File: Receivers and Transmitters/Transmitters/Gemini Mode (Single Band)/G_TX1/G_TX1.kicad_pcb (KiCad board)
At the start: 4 copper layers, 39.8 x 55.8 mm, 37 parts, among them J1 Conn_01x05_Socket, J2 Conn_01x03_Socket, J3 Conn_01x04_Socket, J4 Conn_02x06_Odd_Even, U1 TPS7A4701xRGW, U2 ESP32-WROOM-32, U3 E28-2G4M27S, U4 ESP8285H16, U5 E28-2G4M27S, Y2 26MHz

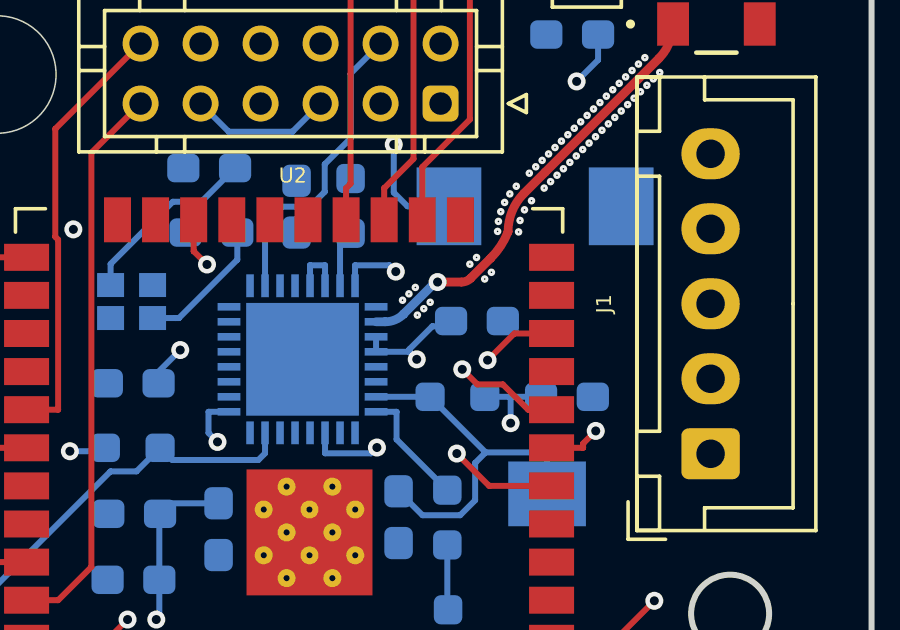
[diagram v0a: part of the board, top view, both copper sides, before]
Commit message: Add Gemini Mode (Single Band) TX board image and documentation updates - Updated hardware setup to include Gemini TX - Added G_TX1_2.4G preview image - Updated KiCad schematic with LNA section and 5.6pF matching capacitor for 50Ω impedance - Modified PCB layout accordingly - Updated README and index.html with Gemini TX board references
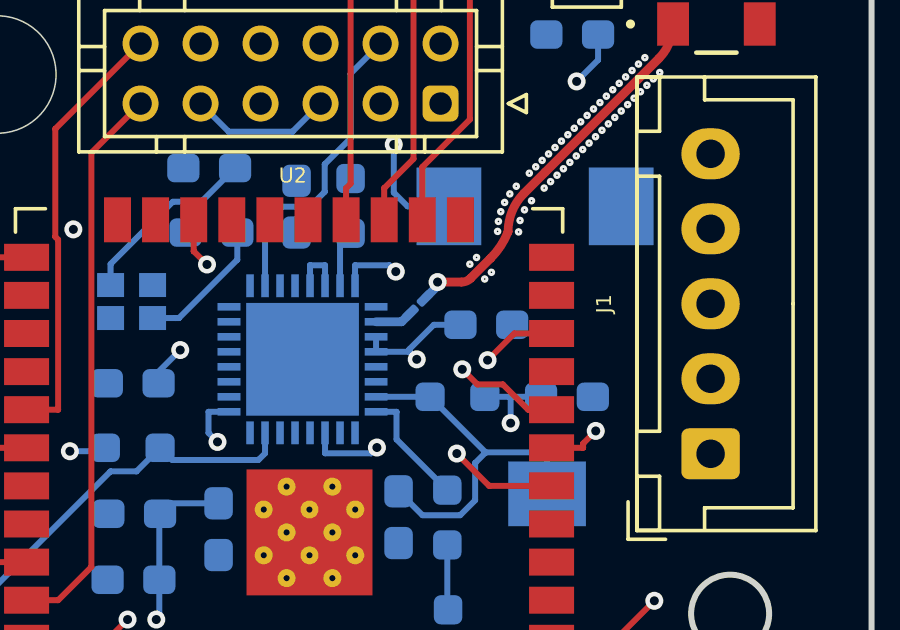
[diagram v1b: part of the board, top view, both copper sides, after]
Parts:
- added C33: 5.6pF, Capacitor_SMD:C_01005_0402Metric_Pad0.57x0.30mm_HandSolder, B.Cu at (153.8, 89.0)
- moved C28 0.34 mm to (156.1, 89.7)
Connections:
- AE1 pad 1: Net-(U4-LNA) -> Net-(AE1-Pad1)
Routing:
- net Net-(U4-LNA): track 14.7 -> 1.27 mm, vias 1 -> 0
- net Net-(AE1-Pad1): track 0.00 -> 13.0 mm, vias 0 -> 1
- net GND: vias 58 -> 52

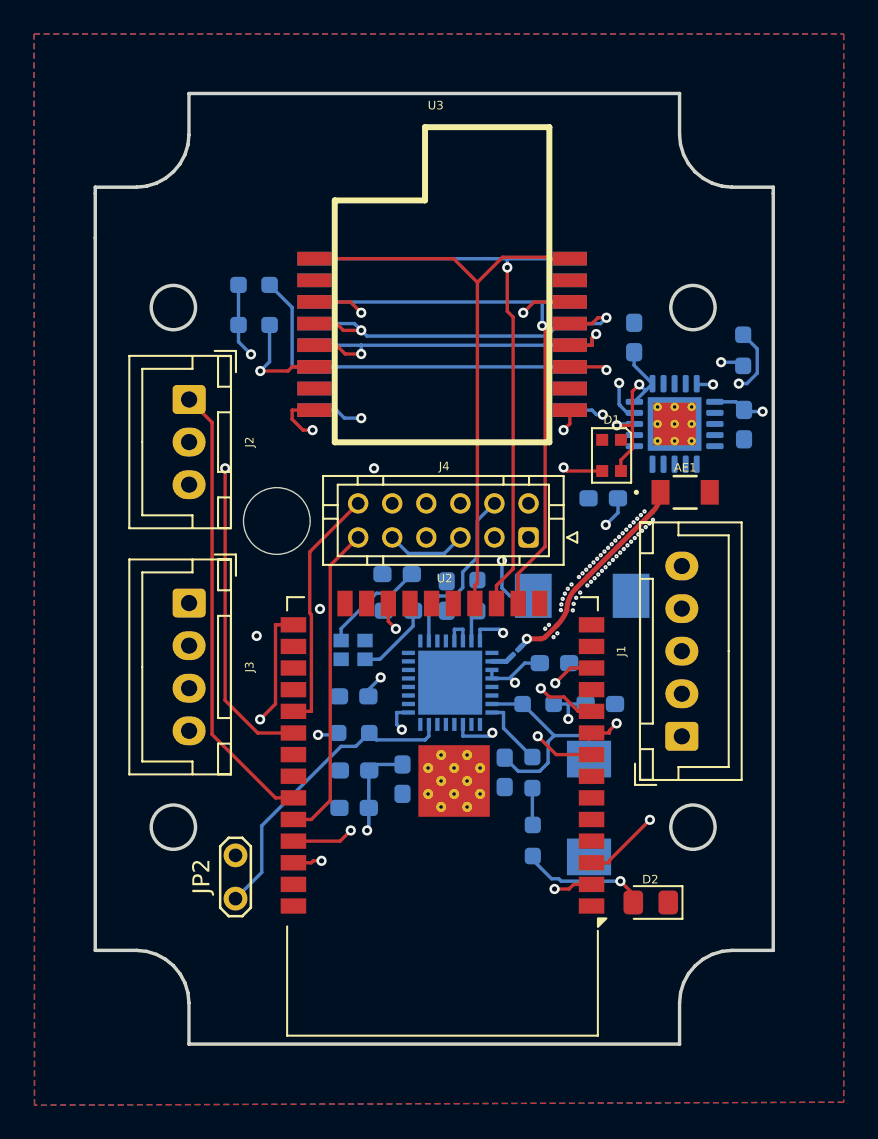
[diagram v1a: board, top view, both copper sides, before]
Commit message: Update Antenna Diversity (AD1_2.4G), True Antenna Diversity (TD1_2.4G), and Gemini Mode transmitter (G_TX1): Modify KiCad files, add BOMs and production files; update images, docs, videos, and README; remove outdated Mechanical CAD file
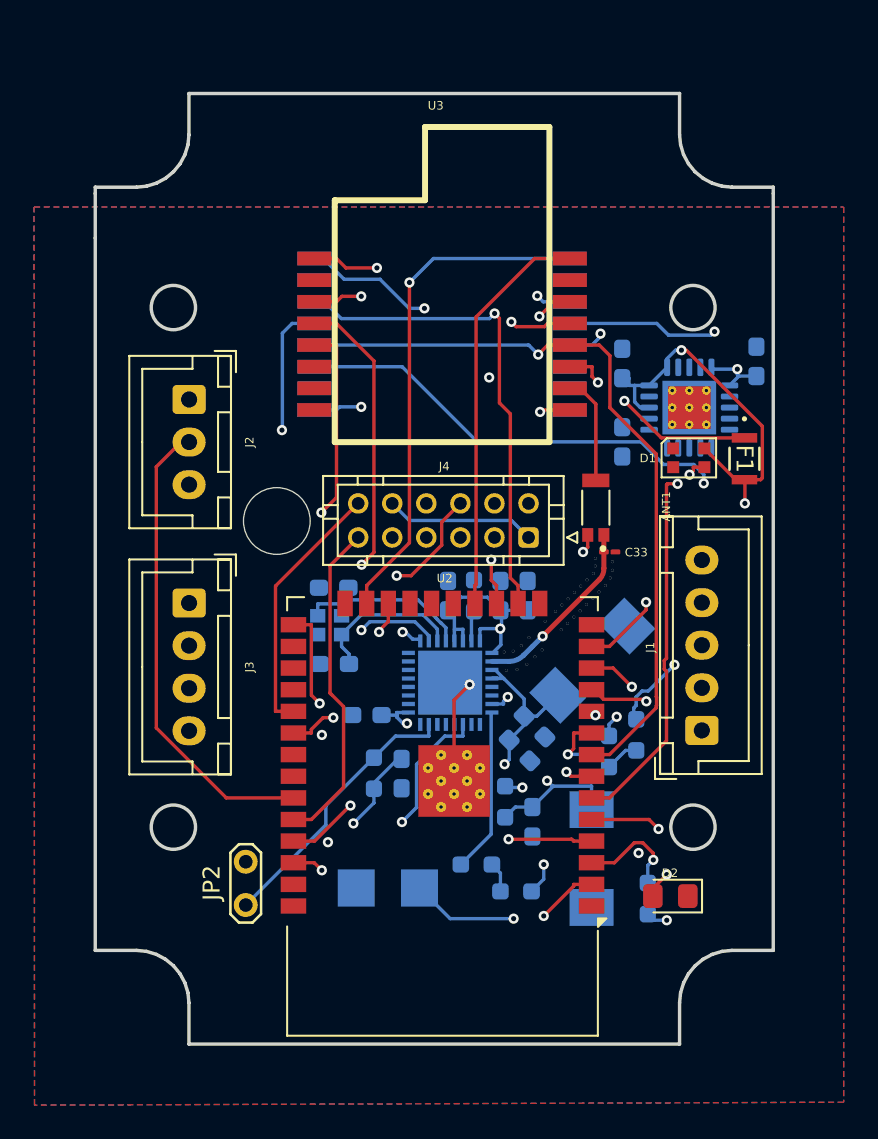
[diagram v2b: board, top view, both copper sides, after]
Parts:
- removed AE1: W3008, W3008:ANT_W3008_PUL
- added ANT1: W3008, W3008:ANTENNA_W3008, F.Cu at (158.5, 80.5)
- added CR1: SMBJ60A, ul_SMBJ60A:SMBJSeries_LTF, B.Cu at (146.3, 102.8)
- added F1: MF-PSMF020X-2, ul_MF-PSMF020X-2:FUSE_F020X_BRN, F.Cu at (167.2, 77.7)
- added QR*****: qrCode, qrlogo:qrCode, B.Cu at (153.5, 108.5)
- C33: value 5.6pF -> 1.5pF; moved to F.Cu
- moved R3 34.7 mm to (160.8, 93.9), turned to -90 degrees
- moved R1 32.7 mm to (161.5, 103.5)
- moved R2 32.6 mm to (159.2, 94.8), turned to -90 degrees
- moved C23 11.8 mm to (154.5, 85.7), turned to 90 degrees
- moved C24 11.6 mm to (149.8, 85.7), turned to 90 degrees
- moved C33 8.07 mm to (159.3, 83.1), turned to 0 degrees
- moved R5 6.32 mm to (151.5, 101.5), turned to 0 degrees
- moved R7 6.06 mm to (153.2, 97.8), turned to -90 degrees
- moved C28 5.52 mm to (154.0, 94.8), turned to -45 degrees
- moved C25 5.50 mm to (145.0, 92.7)
- moved C21 4.89 mm to (143.1, 89.7)
- moved D1 4.54 mm to (163.9, 77.6), turned to 0 degrees
- moved C27 4.08 mm to (154.9, 93.4), turned to -45 degrees
- moved C30 3.85 mm to (158.3, 89.5), turned to -135 degrees
- moved C22 3.81 mm to (143.1, 85.2)
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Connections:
- C1 pad 1: +5V -> /F2
- C33 pad 1: Net-(AE1-Pad1) -> Net-(U4-LNA)
- C33 pad 2: Net-(U4-LNA) -> GND
- D1 pad 4: +5V -> /F2
- J1 pad 1: /BOOT0 -> +3.3V
- J1 pad 2: /TX -> /BOOT0
- J1 pad 3: /RX -> /TX
- J1 pad 4: +3.3V -> /RX
- J2 pad 1: /SPORT -> +5V
- J2 pad 2: +3.3V -> /SPORT
- J3 pad 1: /SCK -> +3.3V
- J3 pad 2: /SDA -> /SCK
- J3 pad 3: +3.3V -> /SDA
- J4 pad 6: /ESP8285/TX -> /ESP8285/RX
- J4 pad 8: /ESP8285/RX -> /ESP8285/TX
- U1 pad 13: +5V -> /F2
- U1 pad 15: +5V -> /F2
- U1 pad 16: +5V -> /F2
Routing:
- net /F2: track 0.00 -> 63.1 mm, vias 0 -> 3
- net /BUSY_1: track 0.00 -> 49.4 mm, vias 0 -> 3
- net /NRESET: track 0.00 -> 47.1 mm, vias 0 -> 3
- net /TX_EN_1: track 0.00 -> 46.2 mm, vias 0 -> 2
- net /BUSY_2: track 0.00 -> 43.8 mm, vias 0 -> 2
- net /DIO1_1: track 0.00 -> 42.0 mm, vias 0 -> 3
- net Net-(U2-IO33): track 46.7 -> 7.18 mm, vias 3 -> 1
- net /DIO1_2: track 0.00 -> 35.1 mm, vias 0 -> 2
- net Net-(U2-EN): track 36.9 -> 6.25 mm, vias 2 -> 1
- net /TX_EN_2: track 0.00 -> 29.9 mm, vias 0 -> 1
- net +5V: track 11.8 -> 35.8 mm, vias 2 -> 1
- net /MISO_2: track 21.7 -> 41.8 mm, vias 0 -> 2
- net /TX_ESP32: track 41.7 -> 26.4 mm
- net Net-(U1-NR): track 13.3 -> 0.00 mm, vias 2 -> 0
- net GND: track 0.00 -> 13.2 mm, vias 52 -> 32
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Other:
- board text added: "G_TX1_2.4G TRANSMITTER BOARD (Gemini Mode Compatible) REV: 1.0 2025-02-23"

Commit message: Update G_TX1 Freecad for enclosure and KiCad files (schematics, PCB, and project) - added fan pin headers
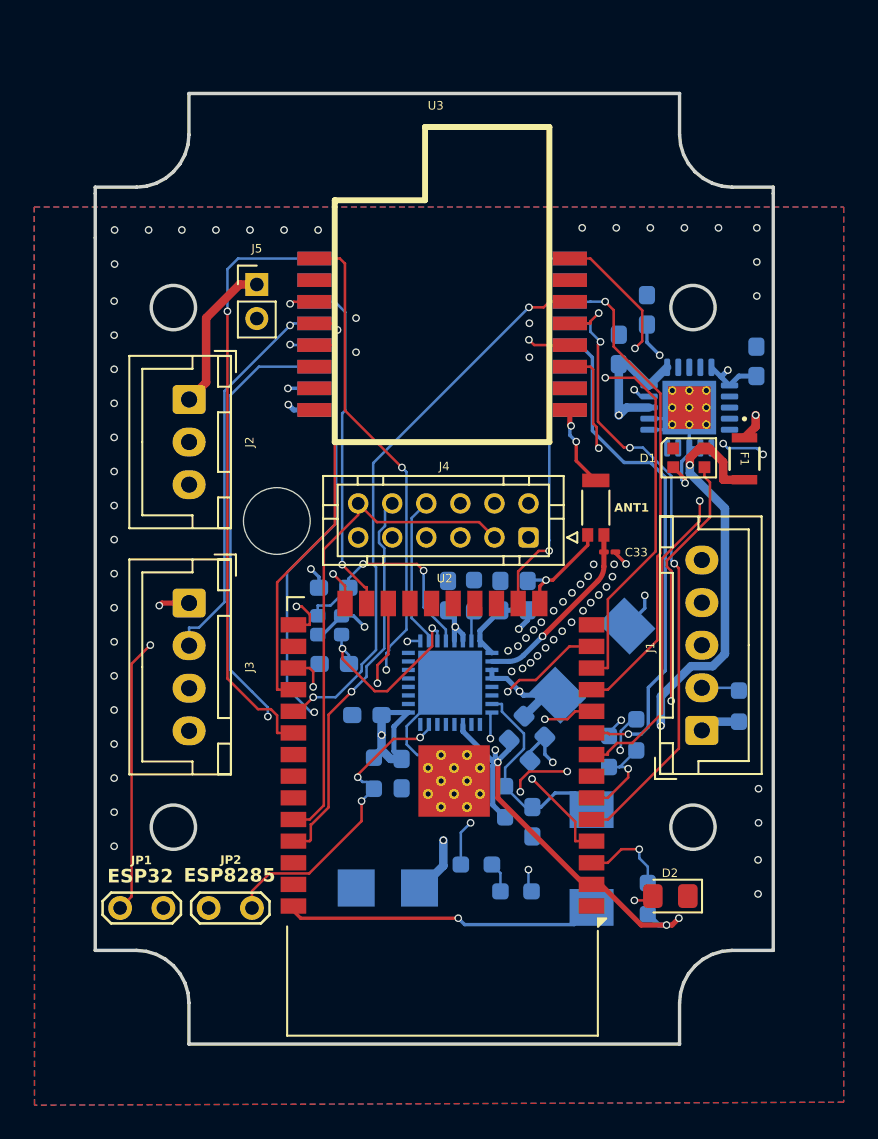
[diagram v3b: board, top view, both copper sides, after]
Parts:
- removed QR*****: qrCode, qrlogo:qrCode
- added J5: Conn_01x02_Pin, Connector_PinHeader_2.00mm:PinHeader_1x02_P2.00mm_Vertical, F.Cu at (138.6, 67.4)
- added JP1: Jumper_2_Small_Bridged, TestPoint:TestPoint_2Pads_Pitch2.54mm_Drill0.8mm, F.Cu at (130.6, 104.0)
- added R9: 10K, Resistor_SMD:R_0603_1608Metric_Pad0.98x0.95mm_HandSolder, B.Cu at (166.9, 92.2)
- moved C2 7.88 mm to (161.5, 68.9), turned to 90 degrees
- moved C1 0.85 mm to (159.8, 71.2)
- moved JP2 0.40 mm to (138.3, 104.0), turned to 180 degrees
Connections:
- R2 pad 2: Net-(U2-IO33) -> Net-(U2-IO34)
- R3 pad 2: Net-(U2-IO33) -> Net-(U2-IO34)
- R7 pad 1: +3.3V -> Net-(U4-CHIP_EN)
- R7 pad 2: Net-(U4-CHIP_EN) -> +3.3V
- R8 pad 1: +3.3V -> Net-(JP2-A)
- R8 pad 2: Net-(JP2-A) -> +3.3V
- U2 pad 12: /NSS_1 -> /RX_EN_1
- U2 pad 16: /NSS_2 -> /TX_EN_2
- U2 pad 17: /RX_EN_2 -> unconnected-(U2-SHD/SD2-Pad17)
- U2 pad 18: /RX_EN_1 -> unconnected-(U2-SWP/SD3-Pad18)
- U2 pad 23: /TX_EN_2 -> /NSS_2
- U2 pad 24: unconnected-(U2-IO2-Pad24) -> /SPORT
- U2 pad 27: unconnected-(U2-IO16-Pad27) -> /LED_RGB
- U2 pad 28: unconnected-(U2-IO17-Pad28) -> /DIO1_1
- U2 pad 29: /RX_ESP32 -> /NSS_1
- U2 pad 30: /TX_ESP32 -> /RX_EN_2
- U2 pad 33: /SPORT -> unconnected-(U2-IO21-Pad33)
- U2 pad 34: /RX -> /RX_ESP32
- U2 pad 35: /TX -> /TX_ESP32
- U2 pad 36: /LED_RGB -> unconnected-(U2-IO22-Pad36)
- U2 pad 6: /DIO1_2 -> Net-(U2-IO34)
- U2 pad 7: /DIO1_1 -> unconnected-(U2-IO35-Pad7)
- U2 pad 9: Net-(U2-IO33) -> /DIO1_2
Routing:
- net GND: track 13.2 -> 60.6 mm, vias 32 -> 76
- net /TX: track 59.8 -> 30.3 mm, vias 1 -> 0
- net /BOOT0: track 29.7 -> 56.4 mm, vias 1 -> 2
- net /DIO1_1: track 42.0 -> 23.8 mm, vias 3 -> 0
- net /MOSI: track 44.8 -> 59.5 mm, vias 1 -> 3
- net /RX: track 47.8 -> 33.4 mm
- net /MISO_1: track 26.3 -> 40.3 mm, vias 2 -> 4
- net /SPORT: track 27.6 -> 15.8 mm, vias 0 -> 1
- net +5V: track 35.8 -> 45.8 mm
- net +3.3V: track 53.1 -> 63.0 mm, vias 11 -> 12
- net /MISO_2: track 41.8 -> 51.6 mm, vias 2 -> 4
- net /NSS_2: track 28.7 -> 19.9 mm
- net /RX_EN_1: track 23.8 -> 31.8 mm, vias 0 -> 2
- net /BUSY_2: track 43.8 -> 35.9 mm, vias 2 -> 3
- net /LED_RGB: track 45.9 -> 38.5 mm, vias 3 -> 2
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- added copper zone on In3.Cu, net GND
- added copper zone on In4.Cu, net GND
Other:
- copper layers 4 -> 6
- board text added: "ESP32"
- board text added: "ESP8285"

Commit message: Update G_TX1: PCB layout, project file, schematic, and README
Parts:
- added G***: LOGO, LOGO, B.Cu at (156.3, 108.7)
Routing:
- net /MOSI: track 59.5 -> 61.9 mm
- net +3.3V: track 63.0 -> 65.2 mm, vias 12 -> 11
- net /NRESET: track 48.8 -> 50.9 mm
- net /RX: track 33.4 -> 35.0 mm
- net /RX_EN_1: track 31.8 -> 30.3 mm
- net Net-(U4-XTAL_IN): track 13.0 -> 11.6 mm
- net Net-(U4-XTAL_OUT): track 11.7 -> 13.0 mm
- net GND: track 60.6 -> 59.6 mm
- net /F2: track 59.5 -> 60.4 mm
- net /ESP8285/RX: track 18.7 -> 19.5 mm
- net /MISO_2: track 51.6 -> 52.4 mm
- net /RX_EN_2: track 35.2 -> 34.4 mm
- net /BUSY_1: track 46.4 -> 47.2 mm
- net /TX_EN_2: track 22.6 -> 23.3 mm
- net /DIO1_2: track 29.9 -> 30.7 mm
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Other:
- board text added: "G_TX1_2.4G TRANSMITTER BOARD (Gemini Mode Compatible) REV: 1.0 2025-08-27"
- board text removed: "G_TX1_2.4G TRANSMITTER BOARD (Gemini Mode Compatible) REV: 1.0 2025-02-23"
